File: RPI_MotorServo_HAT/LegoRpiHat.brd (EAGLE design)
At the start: 65 x 56 mm, 11 parts, among them IC2 LM2576S, U1 A4950ELJTR-T, U2 A4950ELJTR-T, X1 RASPI_BOARD_B+_H

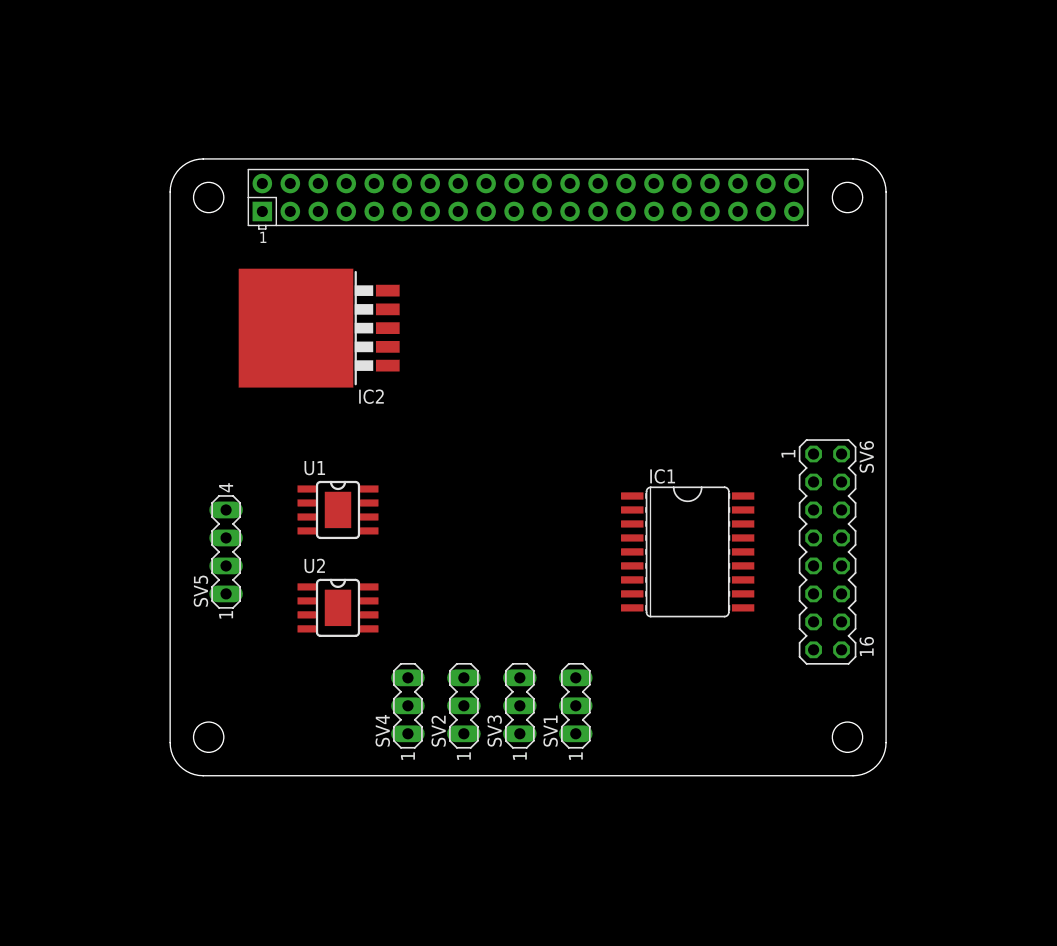
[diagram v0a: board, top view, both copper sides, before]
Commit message: Started to make the connections. Still no passive components added
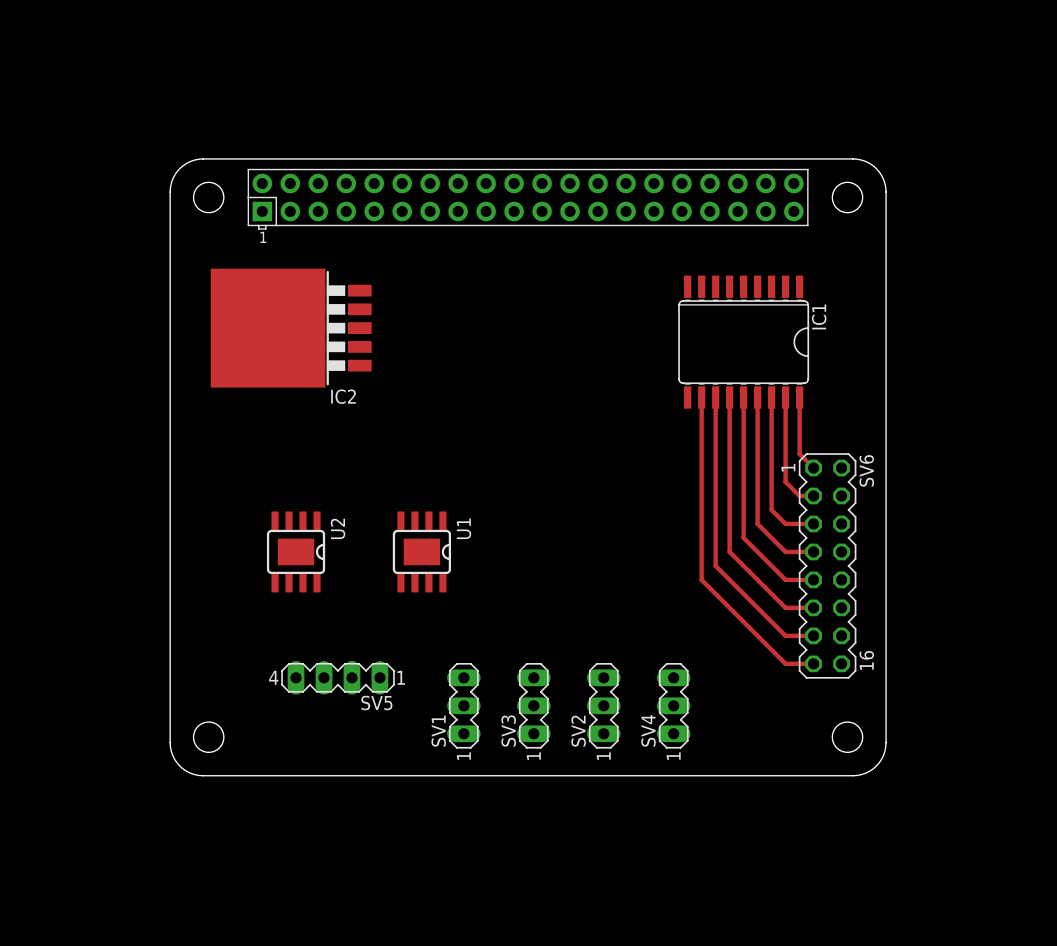
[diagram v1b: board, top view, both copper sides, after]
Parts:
- moved SV4 24.1 mm to (45.7, 6.35)
- moved IC1 19.7 mm to (52.1, 39.4), turned to 180 degrees
- moved SV5 15.3 mm to (15.2, 8.89), turned to 180 degrees
- moved SV2 12.7 mm to (39.4, 6.35)
- moved SV1 10.2 mm to (26.7, 6.35)
- moved U1 8.52 mm to (22.9, 20.3), turned to 270 degrees
- moved U2 6.35 mm to (11.4, 20.3), turned to 270 degrees
- moved IC2 2.54 mm to (11.4, 40.6)
- moved SV3 1.27 mm to (33.0, 6.35)
- moved SV6 1.27 mm to (59.7, 19.1)
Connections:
- removed net 3V3: X1.1
- removed net 5V0: X1.2
- new net GOUT1: IC1.1, X1.40
- new net GOUT2: IC1.2, X1.38
- new net GOUT3: IC1.3, X1.37
- new net GOUT4: IC1.4, X1.36
- new net GOUT5: IC1.5, X1.31
- new net GOUT6: IC1.6, X1.29
- new net GOUT7: IC1.7, X1.28
- new net GOUT8: IC1.8, X1.27
- new net N$1: IC1.18, SV6.1
- new net N$10: SV5.1, U1.8
- new net N$11: SV5.4, U2.6
- new net N$12: SV5.3, U2.8
- new net N$2: IC1.17, SV6.3
- new net N$3: IC1.16, SV6.5
- new net N$4: IC1.15, SV6.7
- new net N$5: IC1.14, SV6.9
- new net N$6: IC1.13, SV6.11
- new net N$7: IC1.12, SV6.13
- new net N$8: IC1.11, SV6.15
- new net N$9: SV5.2, U1.6
- new net PWM0_A: U1.3, X1.32
- new net PWM0_B: U1.2, X1.33
- new net PWM1_A: U2.3, X1.12
- new net PWM1_B: U2.2, X1.35
- new net SERVO1: SV1.3, X1.15
- new net SERVO2: SV2.3, X1.16
- new net SERVO3: SV3.3, X1.18
- new net SERVO4: SV4.3, X1.22
- new net VBATT: U1.5, U2.5
- new net VDD33: U1.4, U2.4, X1.1, X1.17
- new net VDD50: IC1.10, SV1.2, SV2.2, SV3.2, SV4.2, SV6.10, SV6.12, SV6.14, SV6.16, SV6.2, SV6.4, SV6.6, SV6.8, X1.2, X1.4
- net GND: now also SV1.1, SV2.1, SV3.1, SV4.1, U1.1, U1.PAD, U2.1, U2.7, U2.PAD, X1.14, X1.20, X1.25, X1.30, X1.34, X1.39, X1.9
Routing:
- net N$8: track 0.00 -> 29.9 mm
- net N$7: track 0.00 -> 26.8 mm
- net N$6: track 0.00 -> 23.7 mm
- net N$5: track 0.00 -> 20.7 mm
- net N$4: track 0.00 -> 17.6 mm
- net N$3: track 0.00 -> 14.5 mm
- net N$2: track 0.00 -> 10.7 mm
- net N$1: track 0.00 -> 6.93 mm

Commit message: mostly done with the schematics and the component placements. Only missing a couple of components on the 5V regulator
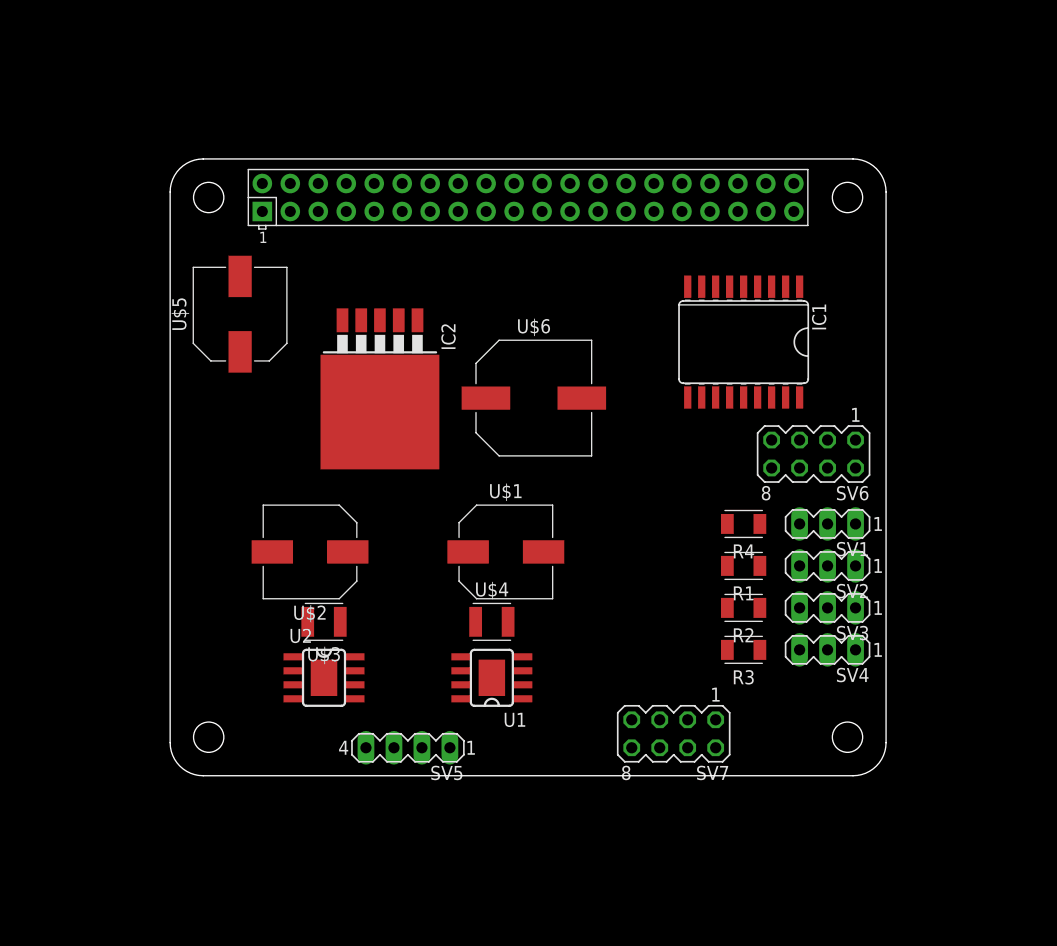
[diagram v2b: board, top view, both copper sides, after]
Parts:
- added R1, R2, R3, R4: (no value), Resistor:RESC3216X70
- added SV7: (no value), con-lstb:MA04-2
- added U$1, U$2, U$5: C-POL_ECAP-8.5MM, Capacitor:CAPAE830X1050N
- added U$3, U$4: C_CHIP-1210(3225-METRIC), Capacitor:CAPC3225X135
- added U$6: C-POL_ECAP-10.5MM, Capacitor:CAPAE1030X1050N
- SV6: device con-lstb:MA08-2 -> con-lstb:MA04-2
- moved SV1 36.9 mm to (59.7, 22.9), turned to 180 degrees
- moved SV3 28.1 mm to (59.7, 15.2), turned to 180 degrees
- moved SV2 24.0 mm to (59.7, 19.1), turned to 180 degrees
- moved SV4 14.9 mm to (59.7, 11.4), turned to 180 degrees
- moved U1 13.1 mm to (29.2, 8.89), turned to 180 degrees
- moved U2 11.7 mm to (14.0, 8.89), turned to 0 degrees
- moved SV6 10.2 mm to (58.4, 29.2), turned to 180 degrees
- moved IC2 9.16 mm to (19.1, 35.6), turned to 180 degrees
- moved SV5 8.98 mm to (21.6, 2.54)
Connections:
- removed net GOUT5: IC1.5, X1.31
- removed net GOUT6: IC1.6, X1.29
- removed net GOUT7: IC1.7, X1.28
- removed net GOUT8: IC1.8, X1.27
- removed net N$5: IC1.14, SV6.9
- removed net N$6: IC1.13, SV6.11
- removed net N$7: IC1.12, SV6.13
- removed net N$8: IC1.11, SV6.15
- removed net VIN: IC2.1
- new net GIN1: SV7.1, X1.31
- new net GIN2: SV7.3, X1.29
- new net GIN3: SV7.5, X1.28
- new net GIN4: SV7.7, X1.27
- new net S1: IC1.14, R4.1, SV1.3
- new net S2: IC1.13, R1.1, SV2.3
- new net S3: IC1.12, R2.1, SV3.3
- new net S4: IC1.11, R3.1, SV4.3
- net GND: now also IC2.5, SV7.2, SV7.4, SV7.6, SV7.8, U$1.2, U$2.2, U$3.2, U$4.2, U$5.2, U$6.2
- net SERVO1: now also IC1.5; no longer SV1.3
- net SERVO2: now also IC1.6; no longer SV2.3
- net SERVO3: now also IC1.7; no longer SV3.3
- net SERVO4: now also IC1.8; no longer SV4.3
- net VBATT: now also IC2.1, U$1.1, U$2.1, U$3.1, U$4.1, U$5.1
- net VDD50: now also IC2.4, R1.2, R2.2, R3.2, R4.2, U$6.1; no longer SV6.10, SV6.12, SV6.14, SV6.16
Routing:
- net N$8: track 29.9 -> 0.00 mm
- net N$7: track 26.8 -> 0.00 mm
- net N$6: track 23.7 -> 0.00 mm
- net N$5: track 20.7 -> 0.00 mm
- net N$1: track 17.6 -> 0.00 mm
- net N$2: track 14.5 -> 0.00 mm
- net N$3: track 10.7 -> 0.00 mm
- net N$4: track 6.93 -> 0.00 mm

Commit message: Testing how to generate pcb mill output
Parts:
- removed IC1: (no value), uln-udn_mod:SO18W
- removed R1, R2, R3, R4: (no value), Resistor:RESC3216X70
- removed SV7: (no value), con-lstb:MA04-2
- added D1: MBRS340T3, diode:SMC
- added JP1: (no value), pinhead:1X02
- added L1: DR127, inductors:DR127
- SV6: device con-lstb:MA04-2 -> con-lstb:MA06-1
- moved U$5 31.1 mm to (22.4, 15.2), turned to 270 degrees
- moved U$4 24.4 mm to (53.6, 14.0)
- moved U1 24.4 mm to (53.6, 8.89)
- moved SV5 21.9 mm to (43.4, 3.81)
- moved U$1 21.8 mm to (52.3, 20.3)
- moved U$2 21.8 mm to (34.5, 20.3)
- moved IC2 21.6 mm to (8.89, 16.5)
- moved SV1 20.8 mm to (59.4, 43.7)
- moved SV2 20.6 mm to (59.4, 39.6)
- moved SV3 20.3 mm to (59.4, 35.6)
- moved SV4 20.1 mm to (59.4, 31.5)
- moved U$3 19.3 mm to (33.3, 14.0)
- moved U2 19.3 mm to (33.3, 8.89)
- moved SV6 17.0 mm to (44.5, 38.9), turned to 270 degrees
- moved U$6 7.78 mm to (28.2, 40.4)
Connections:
- removed net GIN1: SV7.1, X1.31
- removed net GIN2: SV7.3, X1.29
- removed net GIN3: SV7.5, X1.28
- removed net GIN4: SV7.7, X1.27
- removed net GOUT1: IC1.1, X1.40
- removed net GOUT2: IC1.2, X1.38
- removed net GOUT3: IC1.3, X1.37
- removed net GOUT4: IC1.4, X1.36
- removed net N$1: IC1.15, SV6.7
- removed net N$2: IC1.16, SV6.5
- removed net N$3: IC1.17, SV6.3
- removed net N$4: IC1.18, SV6.1
- removed net S1: IC1.14, R4.1, SV1.3
- removed net S2: IC1.13, R1.1, SV2.3
- removed net S3: IC1.12, R2.1, SV3.3
- removed net S4: IC1.11, R3.1, SV4.3
- new net N$5: D1.C, IC2.2, L1.1
- new net SCL: SV6.1, X1.5
- new net SDA: SV6.2, X1.3
- net GND: now also D1.A, JP1.1, SV6.3, U1.7; no longer IC1.9, SV7.2, SV7.4, SV7.6, SV7.8
- net SERVO1: now also SV1.3, X1.40; no longer IC1.5, X1.15
- net SERVO2: now also SV2.3, X1.38; no longer IC1.6, X1.16
- net SERVO3: now also SV3.3, X1.37; no longer IC1.7, X1.18
- net SERVO4: now also SV4.3, X1.36; no longer IC1.8, X1.22
- net VBATT: now also JP1.2, SV6.6
- net VDD33: now also SV6.4; no longer U1.4, U2.4
- net VDD50: now also L1.2, SV6.5, U1.4, U2.4; no longer IC1.10, R1.2, R2.2, R3.2, R4.2, SV6.2, SV6.4, SV6.6, SV6.8
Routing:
- net GND: track 0.00 -> 293.8 mm, vias 0 -> 8
- net VDD50: track 0.00 -> 179.0 mm, vias 0 -> 5
- net VBATT: track 0.00 -> 123.0 mm, vias 0 -> 6
- net PWM1_B: track 0.00 -> 65.2 mm, vias 0 -> 2
- net PWM0_A: track 0.00 -> 62.7 mm, vias 0 -> 2
- net PWM0_B: track 0.00 -> 59.6 mm, vias 0 -> 2
- net PWM1_A: track 0.00 -> 50.1 mm
- net VDD33: track 0.00 -> 50.0 mm, vias 0 -> 2
- net SDA: track 0.00 -> 37.1 mm, vias 0 -> 2
- net SCL: track 0.00 -> 34.3 mm, vias 0 -> 2
- net SERVO4: track 0.00 -> 24.5 mm
- net N$5: track 0.00 -> 20.4 mm
- net SERVO3: track 0.00 -> 16.8 mm
- net SERVO2: track 0.00 -> 15.3 mm
- net N$12: track 0.00 -> 11.7 mm
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- added copper zone on layer 1, net GND
- added copper zone on layer 16, net GND
- added copper zone on layer 16, net _OUTLINES_
- added copper zone on layer 1, net ~_REAL_OUTLINEMILL_~
